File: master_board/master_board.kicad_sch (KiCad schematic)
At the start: 1 part

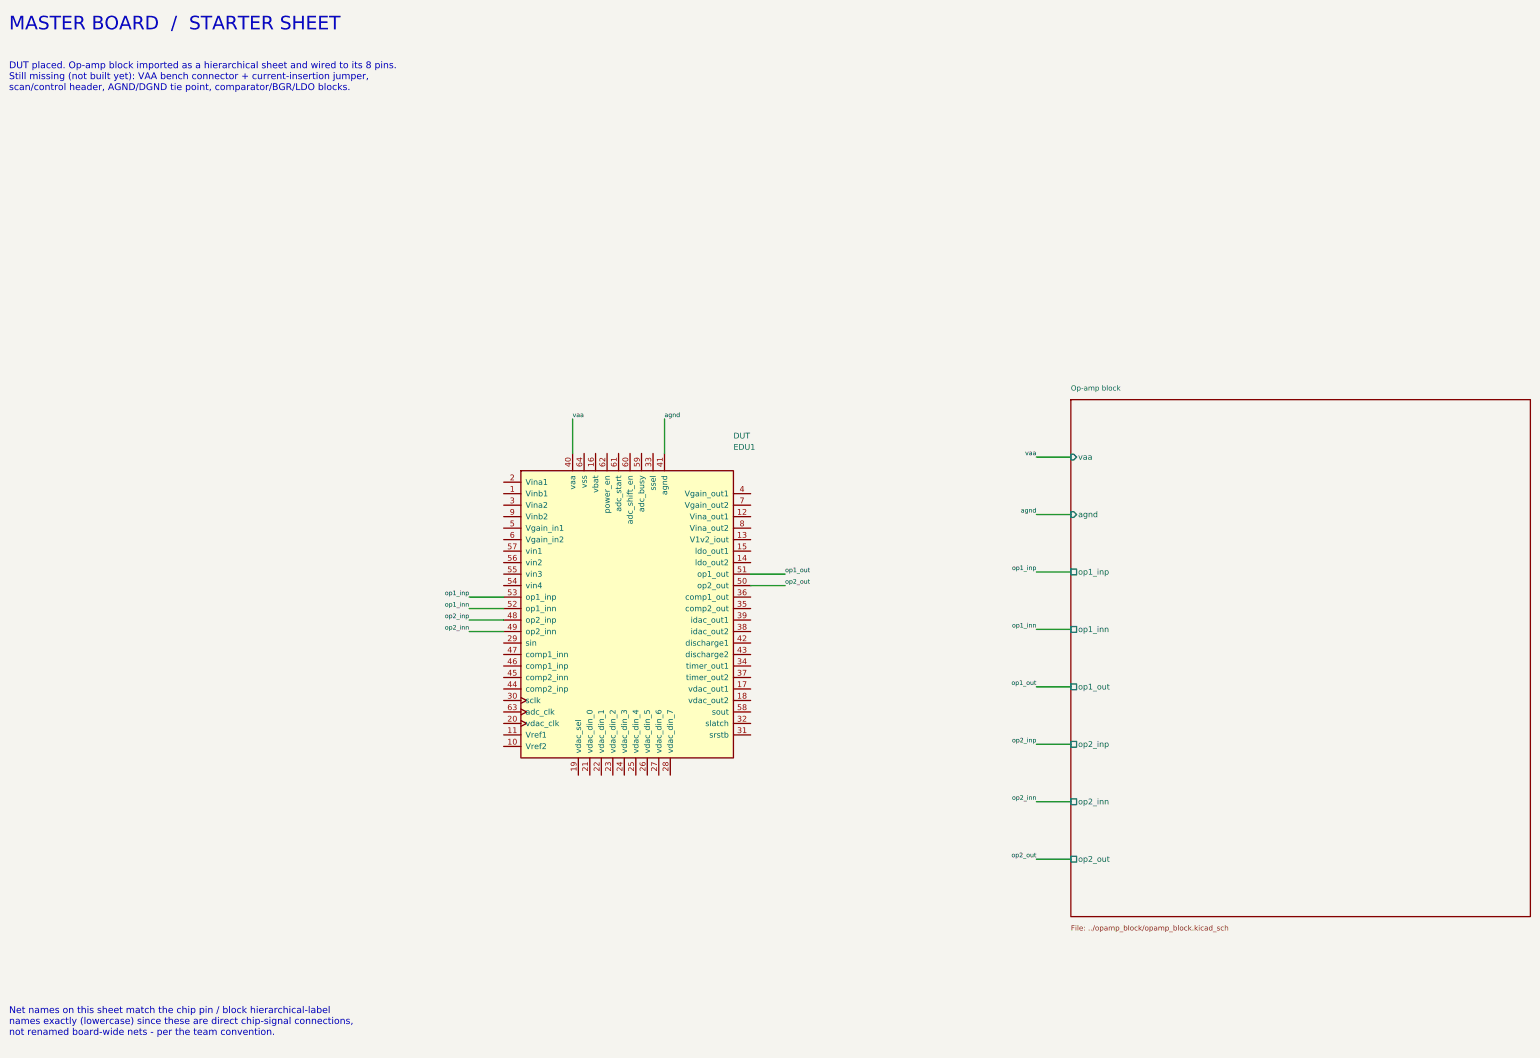
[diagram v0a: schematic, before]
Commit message: Update master_board for flat op-amp block rebuild
- Sheetfile now points to opamp_block/opamp_flat.kicad_sch (renamed
  from opamp_block.kicad_sch in the flat rebuild)
- Added discharge2/timer_out2 sheet pins and wired them to the
  matching DUT pins, since the flat schematic now exposes all 10
  chip-facing signals (previously only 8 were wired)
- Enlarged the sheet symbol to fit the 2 new pins

Co-Authored-By: Claude Sonnet 5 <noreply@anthropic.com>
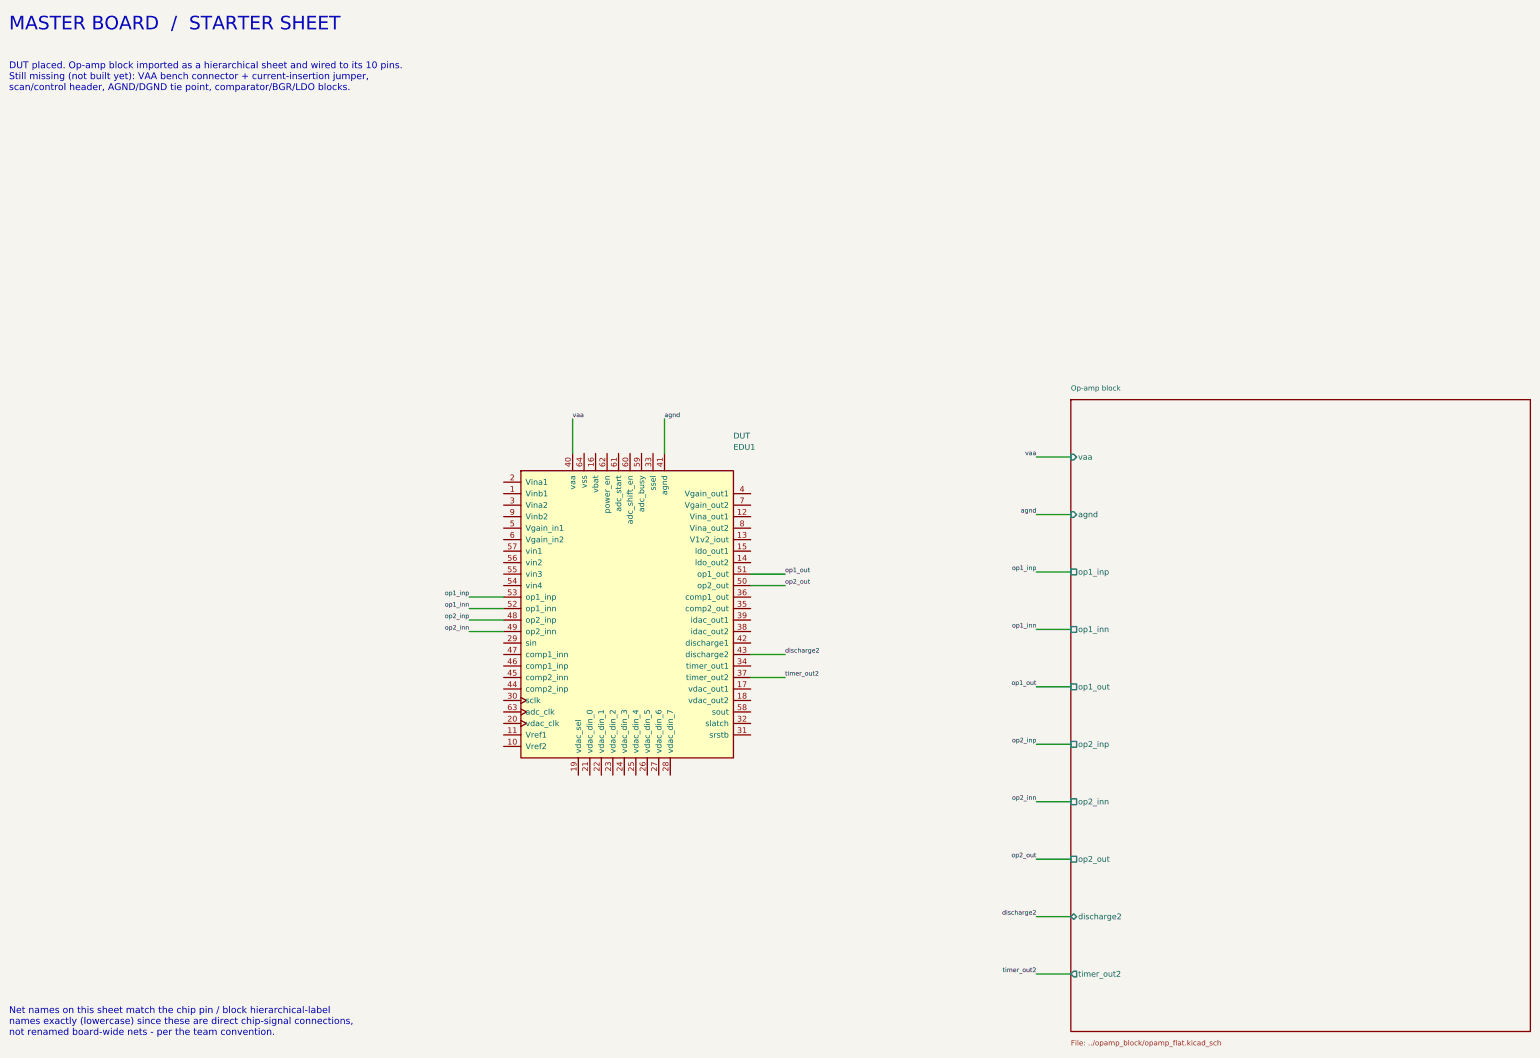
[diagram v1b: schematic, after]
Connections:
- net timer_out2: now reaches DUT.37 (timer_out2)
- net discharge2: now reaches DUT.43 (discharge2)
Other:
- sheet Op-amp block: file ../opamp_block/opamp_block.kicad_sch -> ../opamp_block/opamp_flat.kicad_sch
- sheet Op-amp block ports: added discharge2, timer_out2; removed none
- note added: "DUT placed. Op-amp block imported as a hierarchical sheet and wired to its 10 pins. Still missing (not built yet): VAA bench connector + current-insertion jumper, scan/control header, AGND/DGND tie point, comparator/BGR/LDO blocks."
- note removed: "DUT placed. Op-amp block imported as a hierarchical sheet and wired to its 8 pins. Still missing (not built yet): VAA bench connector + current-insertion jumper, scan/control header, AGND/DGND tie point, comparator/BGR/LDO blocks."
